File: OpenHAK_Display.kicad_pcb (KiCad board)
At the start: 2 copper layers, 21 x 21.6 mm, 10 parts, among them P1 CONN_01X08

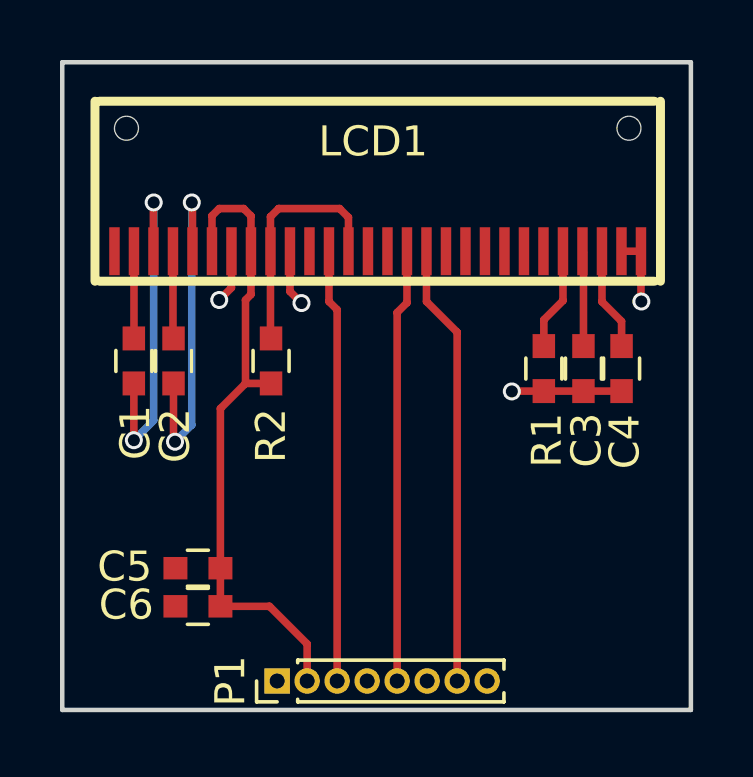
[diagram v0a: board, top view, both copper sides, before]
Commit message: Connect pin 17 to pin 18 to make it work
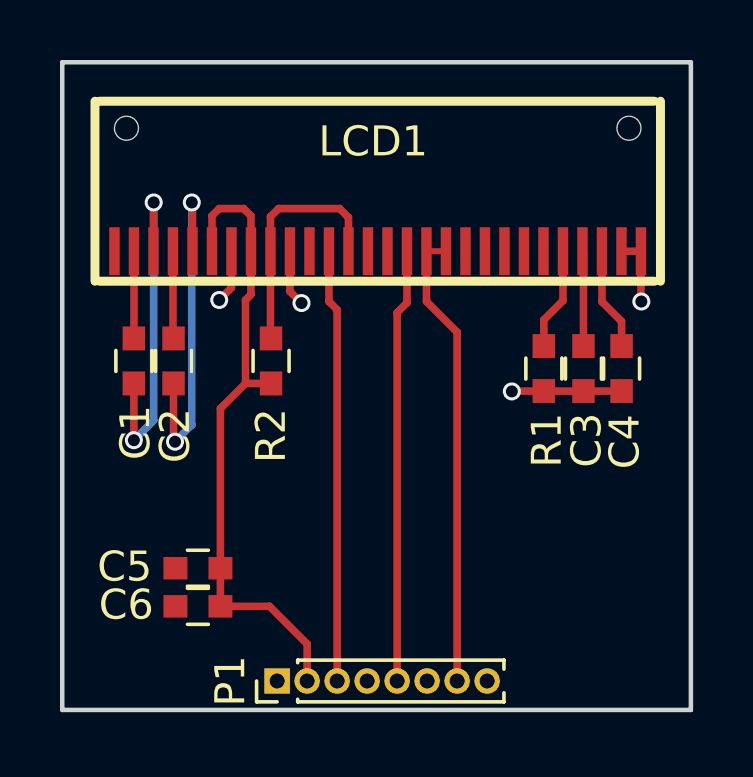
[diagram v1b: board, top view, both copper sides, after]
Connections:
- LCD1 pad 18: Net-(LCD1-Pad18) -> /SDA
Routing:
- net /SDA: track 14.7 -> 15.4 mm
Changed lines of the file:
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@@
 (kicad_pcb (version 4) (host pcbnew 4.0.6)
   (general
-    (links 27)
+    (links 28)
     (no_connects 0)
     (area 103.731287 82.263 154.840715 113.669133)
     (thickness 1.6)
     (drawings 9)
-    (tracks 73)
+    (tracks 74)
     (zones 0)
     (modules 10)
-    (nets 26)
+    (nets 25)
   )
   (page A4)
@@
   )
   (setup
-    (last_trace_width 0.25)
+    (last_trace_width 0.2032)
     (user_trace_width 0.2032)
     (user_trace_width 0.254)
@@
   (net 14 /SCL)
   (net 15 /SDA)
-  (net 16 "Net-(LCD1-Pad18)")
-  (net 17 "Net-(LCD1-Pad19)")
-  (net 18 "Net-(LCD1-Pad20)")
-  (net 19 "Net-(LCD1-Pad21)")
-  (net 20 "Net-(LCD1-Pad22)")
-  (net 21 "Net-(LCD1-Pad23)")
-  (net 22 "Net-(LCD1-Pad24)")
-  (net 23 "Net-(P1-Pad4)")
-  (net 24 "Net-(P1-Pad6)")
-  (net 25 "Net-(P1-Pad8)")
+  (net 16 "Net-(LCD1-Pad19)")
+  (net 17 "Net-(LCD1-Pad20)")
+  (net 18 "Net-(LCD1-Pad21)")
+  (net 19 "Net-(LCD1-Pad22)")
+  (net 20 "Net-(LCD1-Pad23)")
+  (net 21 "Net-(LCD1-Pad24)")
+  (net 22 "Net-(P1-Pad4)")
+  (net 23 "Net-(P1-Pad6)")
+  (net 24 "Net-(P1-Pad8)")
   (net_class Default "This is the default net class."
     (clearance 0.2)
@@
     (add_net "Net-(LCD1-Pad14)")
     (add_net "Net-(LCD1-Pad15)")
-    (add_net "Net-(LCD1-Pad18)")
     (add_net "Net-(LCD1-Pad19)")
     (add_net "Net-(LCD1-Pad20)")
@@
       (net 15 /SDA))
     (pad 18 smd rect (at 2.275 0) (size 0.35 1.6) (layers F.Cu F.Paste F.Mask)
-      (net 16 "Net-(LCD1-Pad18)"))
+      (net 15 /SDA))
     (pad 19 smd rect (at 2.925 0) (size 0.35 1.6) (layers F.Cu F.Paste F.Mask)
-      (net 17 "Net-(LCD1-Pad19)"))
+      (net 16 "Net-(LCD1-Pad19)"))
     (pad 20 smd rect (at 3.575 0) (size 0.35 1.6) (layers F.Cu F.Paste F.Mask)
-      (net 18 "Net-(LCD1-Pad20)"))
+      (net 17 "Net-(LCD1-Pad20)"))
     (pad 21 smd rect (at 4.225 0) (size 0.35 1.6) (layers F.Cu F.Paste F.Mask)
-      (net 19 "Net-(LCD1-Pad21)"))
+      (net 18 "Net-(LCD1-Pad21)"))
     (pad 22 smd rect (at 4.875 0) (size 0.35 1.6) (layers F.Cu F.Paste F.Mask)
-      (net 20 "Net-(LCD1-Pad22)"))
+      (net 19 "Net-(LCD1-Pad22)"))
     (pad 23 smd rect (at 5.525 0) (size 0.35 1.6) (layers F.Cu F.Paste F.Mask)
-      (net 21 "Net-(LCD1-Pad23)"))
+      (net 20 "Net-(LCD1-Pad23)"))
     (pad 24 smd rect (at 6.175 0) (size 0.35 1.6) (layers F.Cu F.Paste F.Mask)
-      (net 22 "Net-(LCD1-Pad24)"))
+      (net 21 "Net-(LCD1-Pad24)"))
     (pad 25 smd rect (at 6.825 0) (size 0.35 1.6) (layers F.Cu F.Paste F.Mask)
       (net 5 "Net-(C3-Pad2)"))
@@
       (net 11 /OLED_RST))
     (pad 4 thru_hole oval (at 0 3 90) (size 0.85 0.85) (drill 0.5) (layers *.Cu *.Mask)
-      (net 23 "Net-(P1-Pad4)"))
+      (net 22 "Net-(P1-Pad4)"))
     (pad 5 thru_hole oval (at 0 4 90) (size 0.85 0.85) (drill 0.5) (layers *.Cu *.Mask)
       (net 14 /SCL))
     (pad 6 thru_hole oval (at 0 5 90) (size 0.85 0.85) (drill 0.5) (layers *.Cu *.Mask)
-      (net 24 "Net-(P1-Pad6)"))
+      (net 23 "Net-(P1-Pad6)"))
     (pad 7 thru_hole oval (at 0 6 90) (size 0.85 0.85) (drill 0.5) (layers *.Cu *.Mask)
       (net 15 /SDA))
     (pad 8 thru_hole oval (at 0 7 90) (size 0.85 0.85) (drill 0.5) (layers *.Cu *.Mask)
-      (net 25 "Net-(P1-Pad8)"))
+      (net 24 "Net-(P1-Pad8)"))
     (model ${KISYS3DMOD}/Pin_Headers.3dshapes/Pin_Header_Straight_1x08_Pitch1.00mm.wrl
       (at (xyz 0 0 0))
@@
       (net 6 GND))
     (pad 1 smd rect (at -0.75 0 270) (size 0.8 0.75) (layers F.Cu F.Paste F.Mask)
-      (net 22 "Net-(LCD1-Pad24)"))
+      (net 21 "Net-(LCD1-Pad24)"))
     (model Capacitors_SMD.3dshapes/C_0603.wrl
       (at (xyz 0 0 0))
@@
   (segment (start 127.6956 96.0276) (end 127.6956 94.3102) (width 0.254) (layer F.Cu) (net 14))
   (segment (start 127.3678 96.3554) (end 127.6956 96.0276) (width 0.254) (layer F.Cu) (net 14))
+  (segment (start 128.9956 94.3102) (end 128.3456 94.3102) (width 0.2032) (layer F.Cu) (net 15) (status C00000))
   (segment (start 129.3678 108.6358) (end 129.3678 97.0082) (width 0.254) (layer F.Cu) (net 15))
   (segment (start 128.3456 95.986) (end 128.3456 94.3102) (width 0.254) (layer F.Cu) (net 15))
   (segment (start 129.3678 97.0082) (end 128.3456 95.986) (width 0.254) (layer F.Cu) (net 15))
-  (segment (start 132.2578 97.4718) (end 132.2578 96.5962) (width 0.254) (layer F.Cu) (net 22))
-  (segment (start 132.8956 95.9584) (end 132.8956 94.3102) (width 0.254) (layer F.Cu) (net 22))
-  (segment (start 132.2578 96.5962) (end 132.8956 95.9584) (width 0.254) (layer F.Cu) (net 22))
+  (segment (start 132.2578 97.4718) (end 132.2578 96.5962) (width 0.254) (layer F.Cu) (net 21))
+  (segment (start 132.8956 95.9584) (end 132.8956 94.3102) (width 0.254) (layer F.Cu) (net 21))
+  (segment (start 132.2578 96.5962) (end 132.8956 95.9584) (width 0.254) (layer F.Cu) (net 21))
   (zone (net 6) (net_name GND) (layer F.Cu) (hatch edge 0.508)
     (connect_pads (clearance 0.254))
